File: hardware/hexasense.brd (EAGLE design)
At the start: 100 x 62 mm, 41 parts

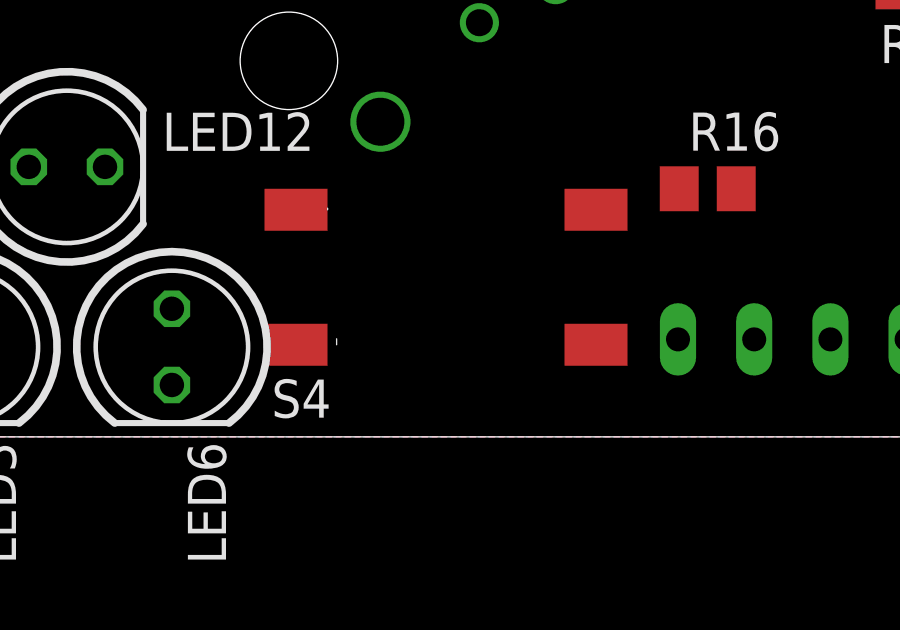
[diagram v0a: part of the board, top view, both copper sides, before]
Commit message: optimized position of reset button
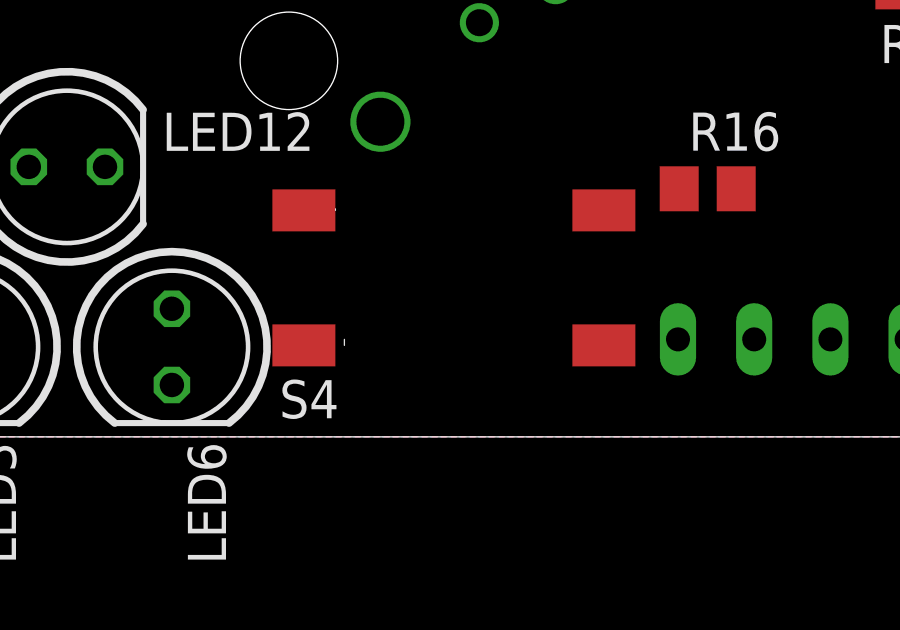
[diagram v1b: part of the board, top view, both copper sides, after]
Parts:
- moved S4 0.26 mm to (30.5, 5.30)
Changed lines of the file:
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@@
 <element name="U$5" library="humidity" package="HUMIDITY-SENSOR" value="HUMIDITY-SENSOR" x="17.23" y="47.53" rot="R270"/>
 <element name="U$6" library="humidity" package="HUMIDITY-SENSOR" value="HUMIDITY-SENSOR" x="54.9" y="40.3" rot="R270"/>
-<element name="S4" library="Ergaenzung" package="TASTER-9314_SMD" value="" x="30.24" y="5.32" smashed="yes">
-<attribute name="NAME" x="24.42" y="0.64" size="1.27" layer="25"/>
-<attribute name="VALUE" x="27.24" y="0.32" size="1.27" layer="27"/>
+<element name="S4" library="Ergaenzung" package="TASTER-9314_SMD" value="" x="30.5" y="5.3" smashed="yes">
+<attribute name="NAME" x="24.68" y="0.62" size="1.27" layer="25"/>
+<attribute name="VALUE" x="27.5" y="0.3" size="1.27" layer="27"/>
 </element>
 <element name="U$7" library="humidity" package="HYT271" value="HYT271" x="15.99" y="47.53" rot="MR90"/>
@@
 <contactref element="U$4" pad="BTN"/>
 <contactref element="S4" pad="1"/>
-<wire x1="25.24" y1="7.57" x2="50.67" y2="18.49" width="0" layer="19" extent="1-1"/>
+<wire x1="25.5" y1="7.55" x2="50.67" y2="18.49" width="0" layer="19" extent="1-1"/>
 </signal>
 <signal name="N$1">

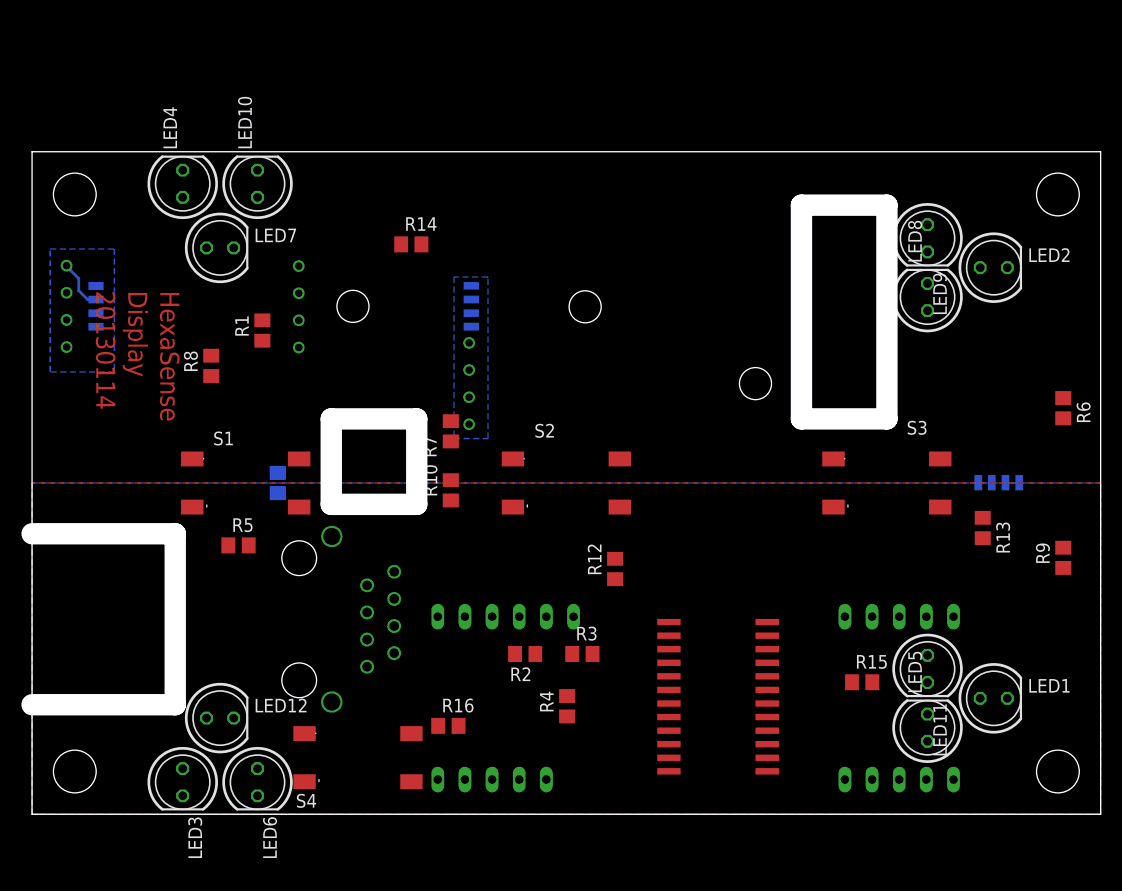
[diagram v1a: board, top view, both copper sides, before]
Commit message: cleaned up position of led resistors and started routing
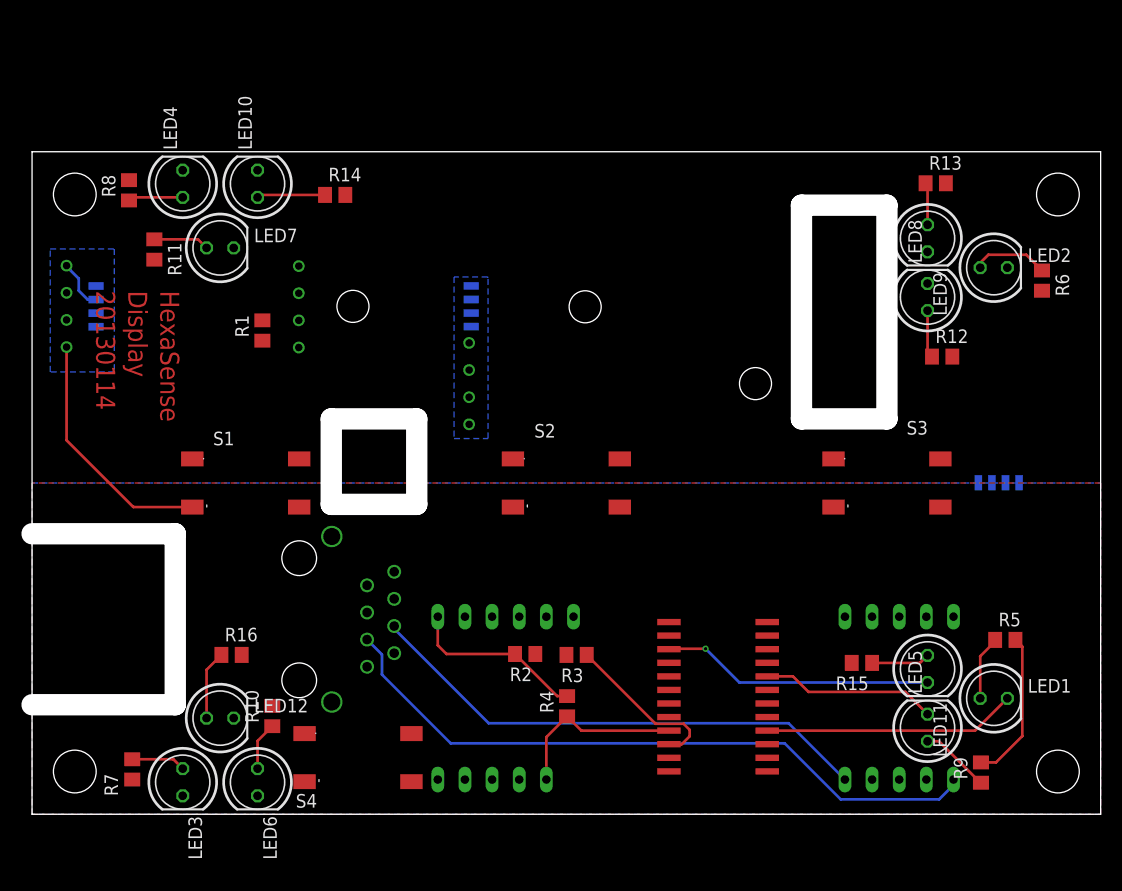
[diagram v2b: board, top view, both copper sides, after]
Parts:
- moved R5 72.3 mm to (91.1, 16.3)
- moved R7 43.5 mm to (9.37, 4.20)
- moved R12 36.5 mm to (85.2, 42.8), turned to 0 degrees
- moved R13 32.6 mm to (84.6, 59.0), turned to 0 degrees
- moved R10 26.9 mm to (22.5, 9.19)
- moved R11 24.7 mm to (11.4, 52.9), flipped to the top
- moved R9 21.5 mm to (88.8, 3.90)
- moved R16 21.3 mm to (18.7, 14.9)
- moved R8 18.1 mm to (9.07, 58.4)
- moved R6 12.1 mm to (94.5, 49.9)
- moved R14 8.49 mm to (28.4, 58.0)
- moved R15 1.80 mm to (77.7, 14.2), turned to 180 degrees
- moved R3 0.55 mm to (51.0, 14.9), turned to 180 degrees
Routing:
- net TEMP_1: track 0.00 -> 63.2 mm
- net TEMP_2: track 0.00 -> 48.3 mm
- net +3V3: track 4.78 -> 35.7 mm
- net N$20: track 0.00 -> 25.5 mm, vias 0 -> 1
- net N$1: track 0.00 -> 23.7 mm
- net GND: track 0.00 -> 23.1 mm
- net !RESET: track 0.00 -> 16.8 mm
- net N$5: track 0.00 -> 16.5 mm
- net SCL: track 0.00 -> 15.4 mm
- net N$11: track 0.00 -> 7.15 mm
- net N$10: track 0.00 -> 7.05 mm
- net N$14: track 0.00 -> 6.61 mm
- net N$24: track 0.00 -> 6.49 mm
- net N$22: track 0.00 -> 6.42 mm
- net N$23: track 0.00 -> 5.48 mm
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
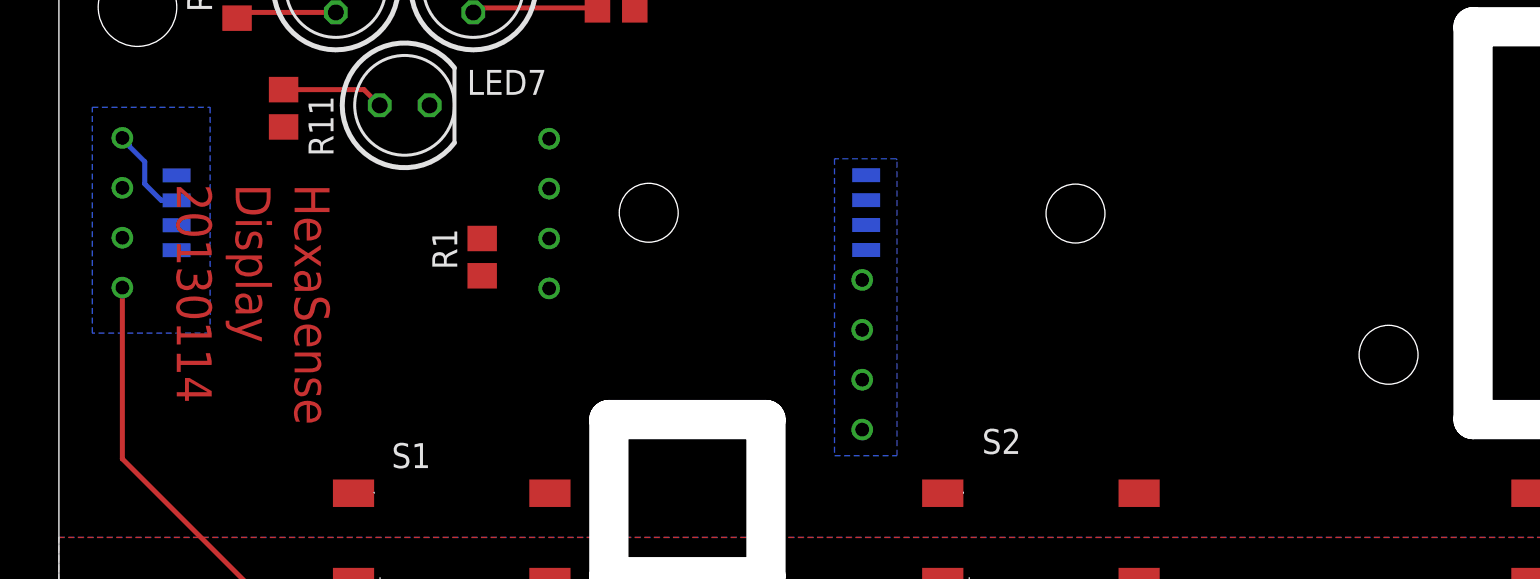
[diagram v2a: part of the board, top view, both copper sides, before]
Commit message: some of the sensors were on the wrong side of the PCB
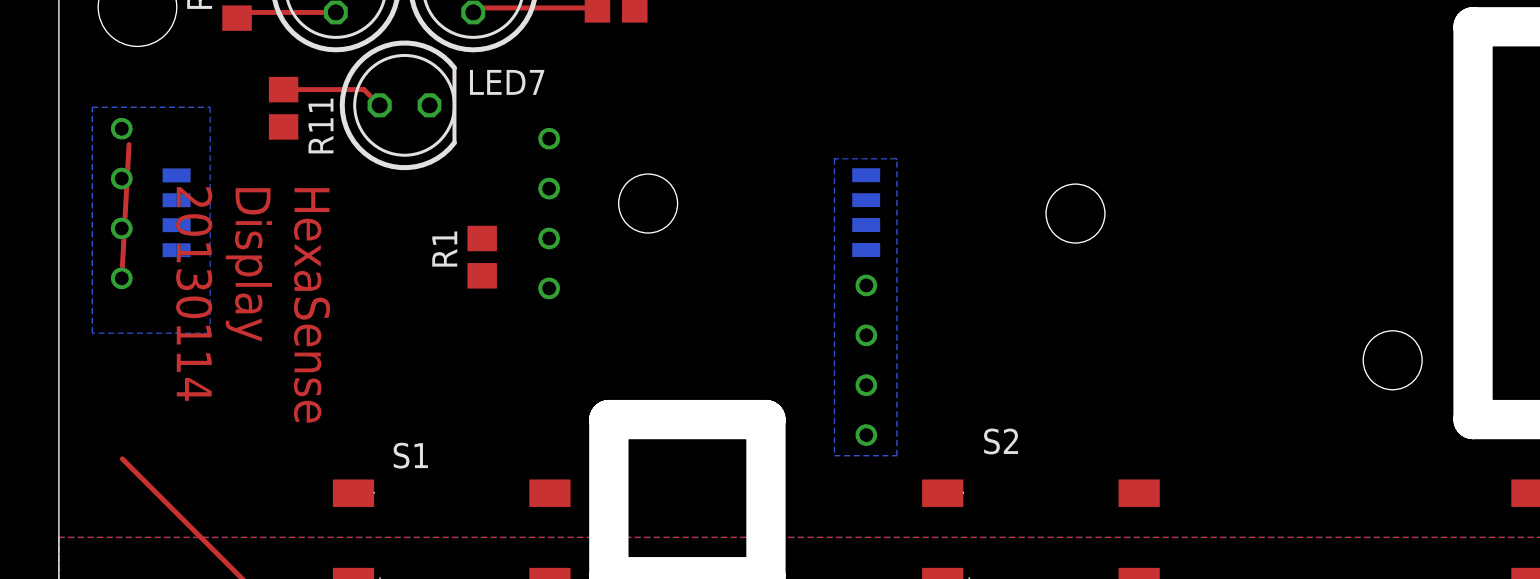
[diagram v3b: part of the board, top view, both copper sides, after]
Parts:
- moved U$5 0.47 mm to (17.2, 48.0), flipped to the bottom, turned to 90 degrees
- moved U$6 0.35 mm to (55.1, 40.0), flipped to the bottom, turned to 90 degrees
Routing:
- net GND: track 23.1 -> 14.4 mm
- net +3V3: track 35.7 -> 37.7 mm
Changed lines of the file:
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@@
 <layer number="42" name="bRestrict" color="1" fill="10" visible="yes" active="yes"/>
 <layer number="43" name="vRestrict" color="2" fill="10" visible="yes" active="yes"/>
-<layer number="44" name="Drills" color="7" fill="1" visible="no" active="yes"/>
+<layer number="44" name="Drills" color="7" fill="1" visible="yes" active="yes"/>
 <layer number="45" name="Holes" color="7" fill="1" visible="yes" active="yes"/>
 <layer number="46" name="Milling" color="3" fill="1" visible="yes" active="yes"/>
@@
 <element name="R4" library="rcl" package="R0805" value="10k" x="50.07" y="10.11" rot="R90"/>
 <element name="U$4" library="hexabus" package="HEXABUS" value="HEXABUS" x="64.2" y="17" rot="MR90"/>
-<element name="U$5" library="humidity" package="HUMIDITY-SENSOR" value="HUMIDITY-SENSOR" x="17.23" y="47.53" rot="R270"/>
-<element name="U$6" library="humidity" package="HUMIDITY-SENSOR" value="HUMIDITY-SENSOR" x="54.9" y="40.3" rot="R270"/>
+<element name="U$5" library="humidity" package="HUMIDITY-SENSOR" value="HUMIDITY-SENSOR" x="17.2" y="48" rot="MR90"/>
+<element name="U$6" library="humidity" package="HUMIDITY-SENSOR" value="HUMIDITY-SENSOR" x="55.11" y="40.02" rot="MR90"/>
 <element name="S4" library="Ergaenzung" package="TASTER-9314_SMD" value="" x="30.5" y="5.3" smashed="yes">
 <attribute name="NAME" x="24.68" y="0.62" size="1.27" layer="25"/>
@@
 <wire x1="15" y1="28.75" x2="9.48" y2="28.75" width="0.254" layer="1"/>
 <wire x1="9.48" y1="28.75" x2="3.23" y2="35" width="0.254" layer="1"/>
-<wire x1="3.23" y1="35" x2="3.23" y2="43.72" width="0.254" layer="1"/>
 <wire x1="24.96" y1="48.76" x2="24.96" y2="51.3" width="0" layer="19" extent="1-1"/>
 <wire x1="41.1" y1="46.905" x2="24.96" y2="48.76" width="0" layer="19" extent="16-16"/>
-<wire x1="45" y1="28.75" x2="40.9" y2="36.49" width="0" layer="19" extent="1-1"/>
+<wire x1="45" y1="28.75" x2="41.11" y2="41.29" width="0" layer="19" extent="1-1"/>
+<wire x1="5.99" y1="46.895" x2="3.23" y2="35" width="0" layer="19" extent="1-16"/>
 </signal>
 <signal name="+3V3">
@@
 <contactref element="U$8" pad="VDD"/>
 <contactref element="U$7" pad="VDD"/>
-<wire x1="5.99" y1="48.165" x2="5.205" y2="48.165" width="0.254" layer="16"/>
-<wire x1="5.205" y1="48.165" x2="4.37" y2="49" width="0.254" layer="16"/>
-<wire x1="4.37" y1="49" x2="4.37" y2="50.13" width="0.254" layer="16"/>
-<wire x1="4.37" y1="50.13" x2="3.57" y2="50.93" width="0.254" layer="16"/>
-<wire x1="3.57" y1="50.93" x2="3.57" y2="51" width="0.254" layer="16"/>
-<wire x1="3.57" y1="51" x2="3.23" y2="51.34" width="0.254" layer="16"/>
+<wire x1="3.57" y1="51" x2="3.2" y2="44.19" width="0.254" layer="1"/>
 <wire x1="45.2" y1="15" x2="49.14" y2="11.06" width="0.254" layer="1"/>
 <wire x1="49.14" y1="11.06" x2="50.07" y2="11.06" width="0.254" layer="1"/>
@@
 <wire x1="22.48" y1="10.14" x2="31.35" y2="13.805" width="0" layer="19" extent="1-1"/>
 <wire x1="9.37" y1="3.25" x2="22.48" y2="10.14" width="0" layer="19" extent="1-1"/>
-<wire x1="40.9" y1="44.11" x2="37.97" y2="18.49" width="0" layer="19" extent="1-1"/>
-<wire x1="41.1" y1="48.175" x2="40.9" y2="44.11" width="0" layer="19" extent="16-16"/>
-<wire x1="24.96" y1="43.68" x2="40.9" y2="44.11" width="0" layer="19" extent="1-1"/>
+<wire x1="41.11" y1="36.21" x2="37.97" y2="18.49" width="0" layer="19" extent="1-1"/>
+<wire x1="41.1" y1="48.175" x2="41.11" y2="36.21" width="0" layer="19" extent="16-16"/>
+<wire x1="24.96" y1="43.68" x2="41.1" y2="48.175" width="0" layer="19" extent="16-16"/>
 <wire x1="21.55" y1="44.32" x2="24.96" y2="43.68" width="0" layer="19" extent="1-1"/>
 <wire x1="11.44" y1="51.9" x2="21.55" y2="44.32" width="0" layer="19" extent="1-1"/>
 <wire x1="5.99" y1="48.165" x2="11.44" y2="51.9" width="0" layer="19" extent="1-16"/>
+<wire x1="3.57" y1="51" x2="5.99" y2="48.165" width="0" layer="19" extent="1-16"/>
 <wire x1="9.07" y1="59.34" x2="11.44" y2="51.9" width="0" layer="19" extent="1-1"/>
 </signal>
@@
 <contactref element="U$5" pad="DATA"/>
 <contactref element="U$6" pad="DATA"/>
-<wire x1="24.96" y1="46.22" x2="40.9" y2="41.57" width="0" layer="19" extent="1-1"/>
+<wire x1="24.96" y1="46.22" x2="41.11" y2="38.75" width="0" layer="19" extent="1-1"/>
 <wire x1="21.55" y1="46.22" x2="24.96" y2="46.22" width="0" layer="19" extent="1-1"/>
-<wire x1="3.23" y1="48.8" x2="21.55" y2="46.22" width="0" layer="19" extent="1-1"/>
-<wire x1="40.51" y1="18.49" x2="40.9" y2="41.57" width="0" layer="19" extent="1-1"/>
+<wire x1="3.2" y1="46.73" x2="21.55" y2="46.22" width="0" layer="19" extent="1-1"/>
+<wire x1="40.51" y1="18.49" x2="41.11" y2="38.75" width="0" layer="19" extent="1-1"/>
 </signal>
 <signal name="SDA">

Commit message: routing...
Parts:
- turned S4 to 180 degrees
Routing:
- net +3V3: track 37.7 -> 279.4 mm, vias 0 -> 2
- net SDA: track 0.00 -> 152.6 mm, vias 0 -> 1
- net +5V: track 0.00 -> 103.2 mm
- net SCL: track 15.4 -> 117.1 mm
- net N$3: track 0.00 -> 63.2 mm
- net N$6: track 0.00 -> 59.5 mm
- net N$21: track 0.00 -> 50.7 mm, vias 0 -> 2
- net DATA: track 0.00 -> 48.7 mm, vias 0 -> 1
- net S3: track 0.00 -> 34.6 mm, vias 0 -> 1
- net BTN: track 0.00 -> 28.3 mm
- net GND: track 14.4 -> 40.5 mm, vias 0 -> 2
